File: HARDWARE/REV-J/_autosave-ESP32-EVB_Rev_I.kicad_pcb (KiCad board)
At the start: 2 copper layers, 75.2 x 74.7 mm, 159 parts, among them CON1 TB3 DG306-5.0-3P, CON2 TB3 DG306-5.0-3P, Q1 BC817-40(SOT23), Q2 BC817-40(SOT23), Q3 Q12MHz/20pF/30ppm/2P/HC-49SM(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, Q4 BC817-40(SOT23), Q5 BC817-40(SOT23), Q6 BC817, Q7 BC817-40(SOT23), U1 BL4054B-42TPRN(SOT23-5), U10 BAT54C(SOT23-3), U2 SY8089AAAC(SOT23-5), U3 ESP-WROOM-32, U4 LAN8710A-EZC(QFN32), U5 CH340T(SSOP20W), U6 MCP2562-E/SN(SOIC-8_150mil), U7 RPM7236-H8, U8 NCP303LSN27T1G(SOT-23-5), U9 BAT54C(SOT23-3)

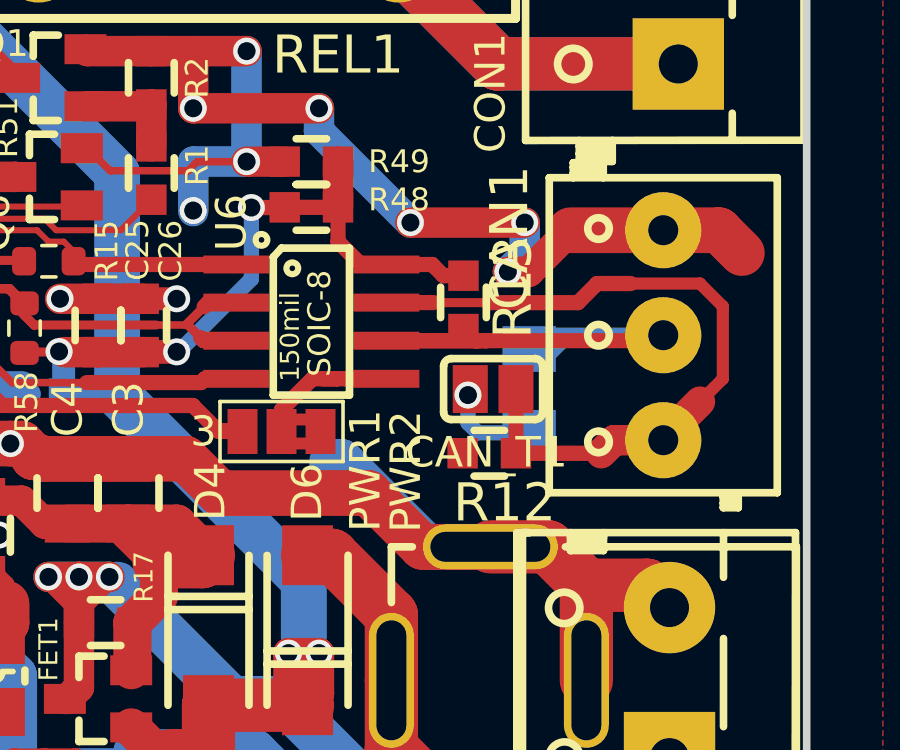
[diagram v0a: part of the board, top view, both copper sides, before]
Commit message: done modbus 485
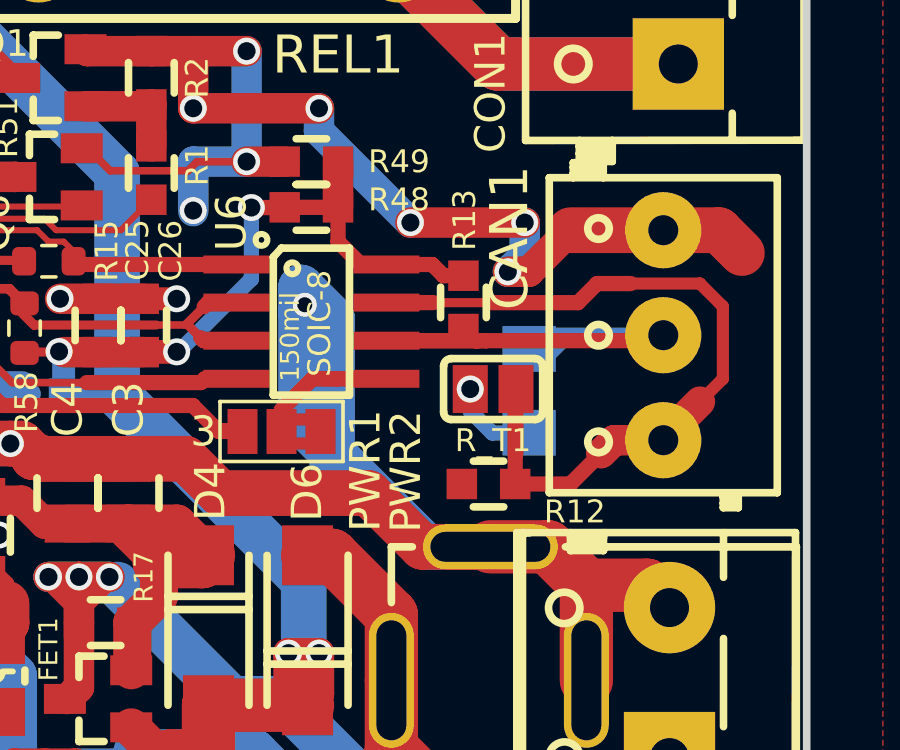
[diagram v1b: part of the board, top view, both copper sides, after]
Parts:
- removed CAN_T1: Opened, OLIMEX_Jumpers-FP:SJ
- added R_T1: Opened, OLIMEX_Jumpers-FP:SJ, F.Cu at (134.3, 112.6)
- moved R12 1.03 mm to (134.2, 115.8)
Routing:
- net GND: track 1005.0 -> 1017.3 mm, vias 133 -> 134
- net /CANH: track 25.9 -> 30.1 mm
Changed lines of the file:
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@@
     (thickness 1.6)
     (drawings 140)
-    (tracks 3311)
+    (tracks 3319)
     (zones 0)
     (modules 159)
@@
     (tags "resistor 0603")
     (attr smd)
-    (fp_text reference R13 (at -0.508 -1.651 90) (layer F.SilkS)
-      (effects (font (size 1.27 1.27) (thickness 0.254)))
+    (fp_text reference R13 (at -2.746 -0.035 90) (layer F.SilkS)
+      (effects (font (size 0.762 0.762) (thickness 0.1905)))
     )
     (fp_text value 10k/R0603 (at 0.127 1.778 90) (layer F.Fab)
@@
   )
   (module OLIMEX_RLC-FP:R_0603_5MIL_DWS (layer F.Cu)
-    (at 134.201 114.75 180)
+    (at 134.175 115.775 180)
     (descr "Resistor SMD 0603, reflow soldering, Vishay (see dcrcw.pdf)")
     (tags "resistor 0603")
     (attr smd)
-    (fp_text reference R12 (at -0.508 -1.651) (layer F.SilkS)
-      (effects (font (size 1.27 1.27) (thickness 0.254)))
+    (fp_text reference R12 (at -2.875 -0.925 180) (layer F.SilkS)
+      (effects (font (size 0.762 0.762) (thickness 0.1905)))
     )
     (fp_text value 10k/R0603 (at 0.127 1.778) (layer F.Fab)
@@
     (tags "SOLDER JUMPER")
     (attr smd)
-    (fp_text reference CAN_T1 (at -0.222 2.11) (layer F.SilkS)
-      (effects (font (size 1.016 1.016) (thickness 0.254)))
+    (fp_text reference R_T1 (at -0.003 1.715) (layer F.SilkS)
+      (effects (font (size 0.762 0.762) (thickness 0.1905)))
     )
     (fp_text value Opened (at -0.127 1.397) (layer F.Fab)
@@
   (via (at 134.82 108.7) (size 0.9) (drill 0.6) (layers F.Cu B.Cu) (net 2))
   (segment (start 135.382 108.138) (end 134.82 108.7) (width 1.016) (layer B.Cu) (net 2))
-  (segment (start 129.264 115.04) (end 128.96 115.04) (width 1.524) (layer B.Cu) (net 2))
-  (segment (start 134.237 117.869) (end 132.093 117.869) (width 1.524) (layer B.Cu) (net 2))
-  (segment (start 132.093 117.869) (end 129.264 115.04) (width 1.524) (layer B.Cu) (net 2))
   (segment (start 119.268512 114.935) (end 124.079 114.935) (width 1.524) (layer F.Cu) (net 2))
   (segment (start 119.217703 114.884191) (end 119.268512 114.935) (width 1.524) (layer F.Cu) (net 2))
@@
   (segment (start 116.58 110.22) (end 117.16 110.8) (width 0.3048) (layer F.Cu) (net 2))
   (segment (start 115.28 110.22) (end 116.58 110.22) (width 0.3048) (layer F.Cu) (net 2))
+  (segment (start 127.925 109.225) (end 128.96 110.26) (width 1.524) (layer B.Cu) (net 2))
+  (segment (start 128.96 110.26) (end 128.96 115.04) (width 1.524) (layer B.Cu) (net 2))
+  (segment (start 127.925 113.701) (end 127.925 110.05) (width 1.524) (layer B.Cu) (net 2))
+  (segment (start 132.093 117.869) (end 127.925 113.701) (width 1.524) (layer B.Cu) (net 2))
+  (segment (start 134.237 117.869) (end 132.093 117.869) (width 1.524) (layer B.Cu) (net 2))
+  (segment (start 127.925 110.05) (end 127.925 109.225) (width 1.524) (layer B.Cu) (net 2))
+  (via (at 128.05 109.8) (size 0.8) (drill 0.5) (layers F.Cu B.Cu) (net 2))
   (segment (start 139.94638 129.53238) (end 136.017 125.603) (width 1.524) (layer B.Cu) (net 3))
   (segment (start 136.017 125.603) (end 129.921 125.603) (width 1.524) (layer B.Cu) (net 3))
@@
   (segment (start 140 114.315) (end 138.365 114.315) (width 1.016) (layer F.Cu) (net 64))
   (segment (start 138.365 114.315) (end 137.93 114.75) (width 1.016) (layer F.Cu) (net 64))
-  (segment (start 135.09 114.75) (end 137.93 114.75) (width 0.508) (layer F.Cu) (net 64))
-  (via (at 133.49 112.81) (size 0.9) (drill 0.6) (layers F.Cu B.Cu) (net 65))
-  (segment (start 133.49 112.81) (end 133.49 113.74) (width 0.508) (layer B.Cu) (net 65))
-  (segment (start 133.817 114.067) (end 135.53 114.067) (width 0.508) (layer B.Cu) (net 65))
-  (segment (start 133.49 113.74) (end 133.817 114.067) (width 0.508) (layer B.Cu) (net 65))
+  (segment (start 135.064 112.636) (end 135.09 112.61) (width 0.508) (layer F.Cu) (net 64))
+  (segment (start 135.064 115.775) (end 135.064 112.636) (width 0.508) (layer F.Cu) (net 64))
+  (segment (start 136.905 115.775) (end 138.365 114.315) (width 0.508) (layer F.Cu) (net 64))
+  (segment (start 135.064 115.775) (end 136.905 115.775) (width 0.508) (layer F.Cu) (net 64))
+  (via (at 133.566 112.609996) (size 0.9) (drill 0.6) (layers F.Cu B.Cu) (net 65))
+  (segment (start 133.566 113.341) (end 133.566 112.609996) (width 0.508) (layer B.Cu) (net 65))
+  (segment (start 134.3 114.075) (end 133.566 113.341) (width 0.508) (layer B.Cu) (net 65))
+  (segment (start 135.522 114.075) (end 134.3 114.075) (width 0.508) (layer B.Cu) (net 65))
+  (segment (start 135.53 114.067) (end 135.522 114.075) (width 0.508) (layer B.Cu) (net 65))
   (via (at 73.025 132.08) (size 0.45) (drill 0.3) (layers F.Cu B.Cu) (net 66))
   (segment (start 105.156 134.874) (end 104.389 134.874) (width 0.2032) (layer F.Cu) (net 66))
